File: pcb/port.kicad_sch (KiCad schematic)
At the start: 0 parts

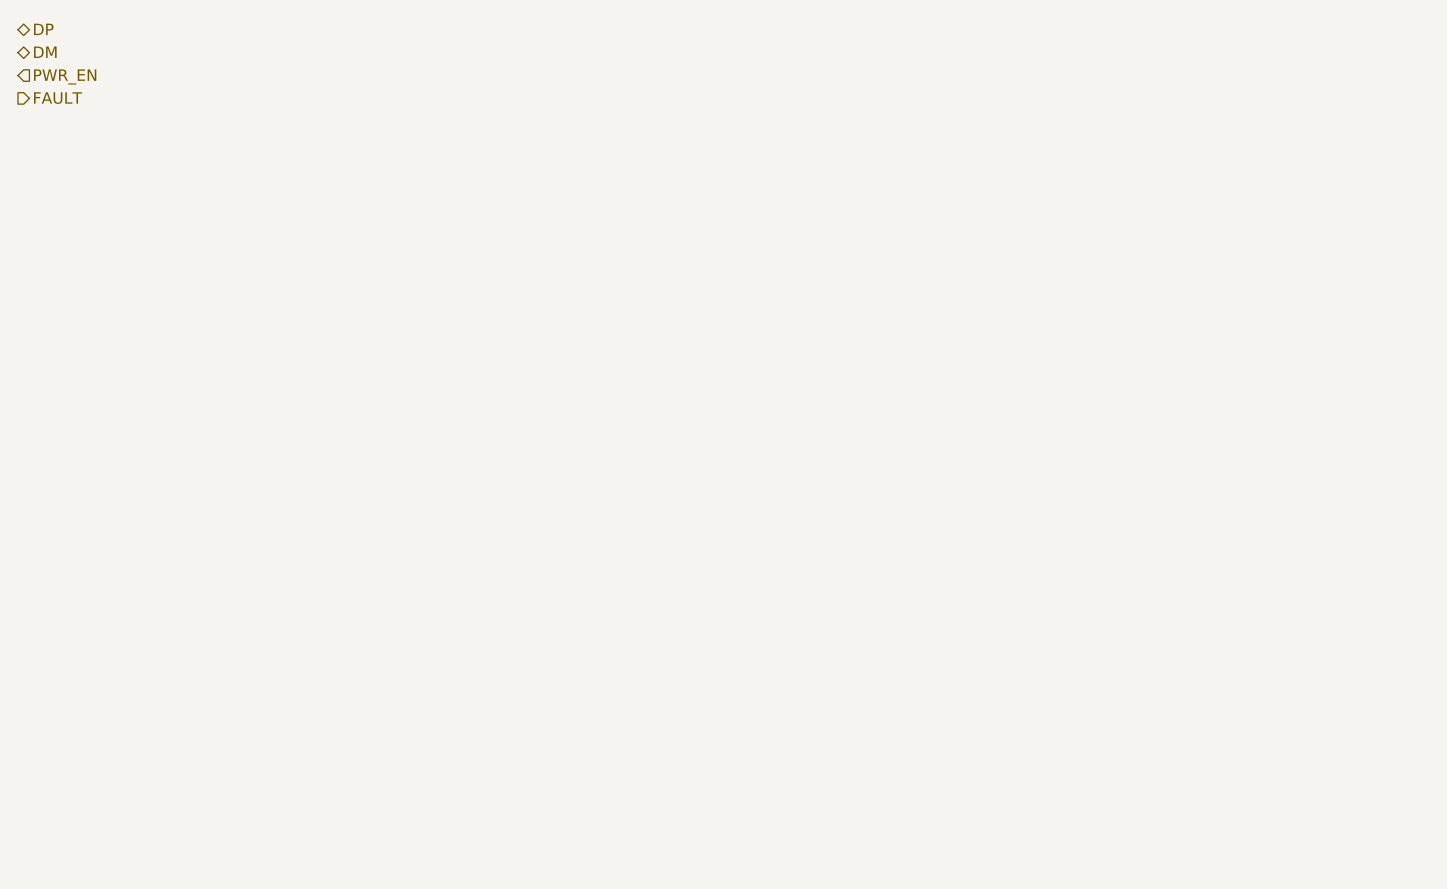
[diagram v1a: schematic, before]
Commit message: draw the port, once, and place it four times
The current-limited switch, the ESD array, the receptacle and the bulk
capacitance. Left to right: the hub's enable arrives, the switch passes 5 V
through, the array protects the pair on its way out, and the receptacle is the
board edge. The fault goes straight back to the hub, which pulls it up itself.

The rails are drawn rather than scattered. Giving every ground pin its own
symbol is quick to generate and tiresome to read -- the sheet fills with
identical glyphs and the shape of the supply disappears -- so the generator now
draws one line, one symbol and a drop to each pin. Same netlist, a tenth of the
symbols. That is the change that was asked for after the same tidying had been
done by hand twice.

Three bugs had to be found on the way, and the first two hid the third.

A symbol may be mirrored, because a connector drawn with its pins facing out of
the package has them facing the wrong way at the right-hand edge of a sheet, and
turning it over instead would reverse the pin order that the pair has to line up
with. The mirror flag was first built as a string of escape sequences and passed
through a plain substitution, which does not interpret them: the literal
characters went into the file, the symbol was malformed, and KiCad stopped
reading the sheet at that point. What it reported was that the sheet had no
hierarchical labels -- which was true, in the sense that it had never got to
them.

The per-placement references then leaked into the reference field itself, which
belongs to one reference; the list belongs only in the instance paths.

And the placements were being read in file order, which the editor is free to
change when it saves -- it had already put them in the order 4, 3, 1, 2. The
references now follow the sheet names, and the generator refuses to run if it
does not find exactly four.

Co-Authored-By: Claude Opus 5 (1M context) <noreply@anthropic.com>
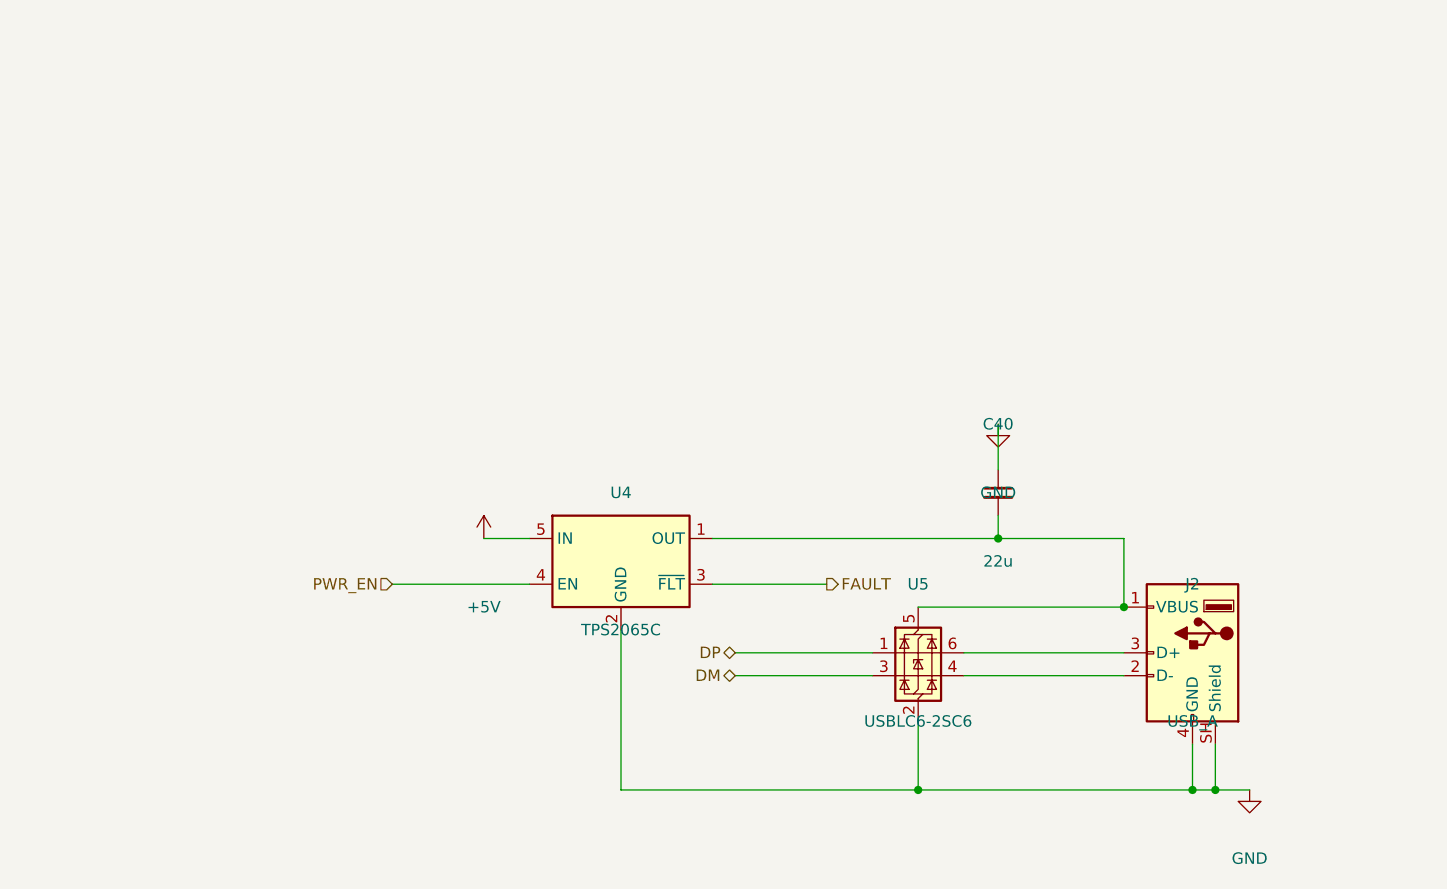
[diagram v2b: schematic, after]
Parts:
- added C40: 22u, symbol Device:C_Small
- added J2: USB_A, symbol Connector:USB_A
- added U4: TPS2065C, symbol Power_Management:TPS2065CDBV
- added U5: USBLC6-2SC6, symbol Power_Protection:USBLC6-2SC6
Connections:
- net DM: now also U5.3 (I/O2)
- net DP: now also U5.1 (I/O1)
- net FAULT: now also U4.3 (~{FLT})
- net PWR_EN: now also U4.4 (EN)
- new net: J2.2 (D-), U5.4 (I/O2)
- new net: C40.2, J2.1 (VBUS), U4.1 (OUT), U5.5 (VBUS)
- new net: J2.3 (D+), U5.6 (I/O1)
- new net +5V: U4.5 (IN)
- new net GND: C40.1, J2.4 (GND), J2.SH (Shield), U4.2 (GND), U5.2 (GND)

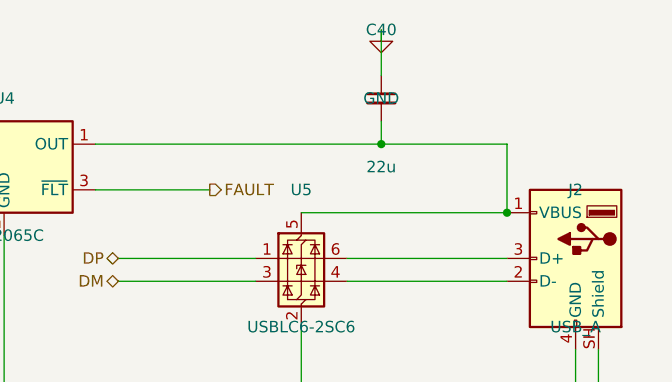
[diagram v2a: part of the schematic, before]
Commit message: draw the data port, and let its pinout answer an open question
The receptacle, the terminations that tell a source what we are, the protection
array, the sense divider the firmware reads to know a host is there, and the
diode through which the rail takes its capped contribution. Both halves of each
data pair are tied, which is what lets the cable go in either way up -- four pin
points, not two, and the netlist is the only place that shows it was done.

Reading the PD sink's pinout to draw the other upstream sheet answered a
question that was down as needing the datasheet by eye. It has no internal
output switch to open: it brings out a gate drive for an external FET. So the
blocking that keeps the data port from back-driving an exposed connector is ours
to design rather than someone else's arrangement to trust, and the open item
becomes an orientation choice. The same pinout shows the requested voltage and
current are resistor-settable as well as addressable, so the profile has a
hardware default before any firmware runs -- worth having on a board whose
firmware is the thing being updated.

The power sheet is NOT drawn, and deliberately. Its three converters each need
numbers this toolchain cannot read: which resistor sets the charger's current
programming against its input-limit pin, and how to tell the boost's feedback
divider apart from its current-limit and frequency resistors. The vendor
publishes both with the pin tables and design equations in a form that extracts
at four and thirty per cent. The topology is understood; the values are not, and
a wrong number in the supply is expensive, so it is recorded as needing a human
with the PDF open rather than drawn from inference.

Co-Authored-By: Claude Opus 5 (1M context) <noreply@anthropic.com>
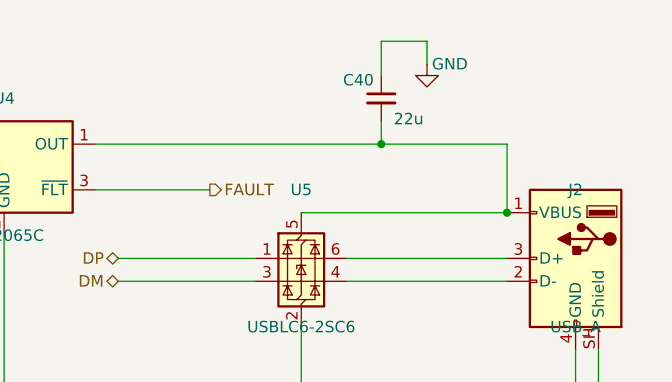
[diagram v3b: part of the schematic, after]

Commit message: specify every capacitor: a rating and a dielectric, chosen from its net
A value on its own is not a specification. Each of the 62 capacitor symbols now carries a voltage
rating and a dielectric picked from the net it sits on -- at least twice the working voltage,
rounded to a standard rating, and never below what a socket the user can reach can present. Both
are hidden fields, so the drawing stays readable and a bill of materials can still be made from it.

Two of the choices are decisions rather than arithmetic.

The connector-side parts are rated for abuse at 50V, because nothing on the board protects them:
both input switches sit downstream of them, so the sink's own supply decoupling and the data
port's see whatever a hostile charger produces with no switch in between.

The charger's input bank is rated 25V on a condition, and the condition is firmware. The input
over-voltage trip defaults to 26V, which is above a 25V part, so rating the bank for its working
voltage is only safe if that trip comes down. The part offers 7V, 12V, 22V and 26V and 12V is the
right one here: the sink never asks for more than 9V, so 12V clears the profile with room and
bounds what the bank can ever see. A board decision that creates a firmware requirement is exactly
the sort that gets lost, so it is recorded on both sides.

What is left open is what the banks are worth once fitted. The charger specifies them as counts of
10uF parts, which only means something if each part is still worth 10uF where it sits, and a
ceramic at 9V is not. The rating and the dielectric are settled; the package is not, and the
package is what decides how much survives. The footprint step has to read each chosen part's bias
curve and add parts if the effective value falls short rather than assume the count was the point.
That is the one piece of this specification that can still change the part count.

Rules check unchanged, and the schematic check is clean.

Co-Authored-By: Claude Opus 5 (1M context) <norepl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
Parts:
- C40: Dielectric (none) -> X7R; Voltage (none) -> 25V
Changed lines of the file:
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@@
+			)
+		)
+		(property "Voltage" "25V"
+			(at 171.958 93.726 0)
+			(show_name no)
+			(do_not_autoplace no)
+			(effects
+				(font
+					(size 1.27 1.27)
+				)
+				(hide yes)
+			)
+		)
+		(property "Dielectric" "X7R"
+			(at 171.958 93.726 0)
+			(show_name no)
+			(do_not_autoplace no)
+			(effects
+				(font
+					(size 1.27 1.27)
+				)
+				(hide yes)
 			)
 		)

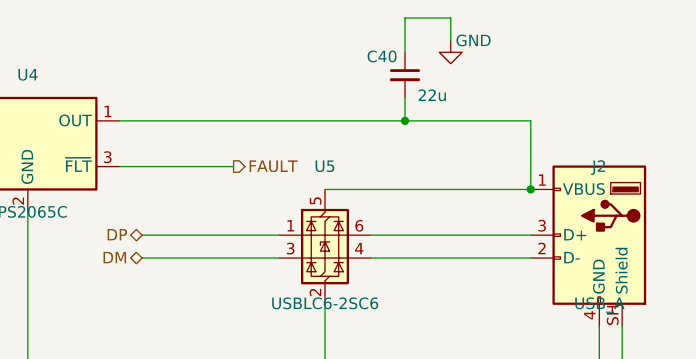
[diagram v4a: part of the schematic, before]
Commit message: calculate the capacitor banks, and give every one of them a package
The question a value and a rating leave open is how much capacitance is actually there once the
voltage is across it, and the answer differs by package for the same value and rating. So the
requirement is derived bank by bank rather than taken from the vendors' part counts.

The charger's input is the binding case. Holding its input ripple to 100 mV with 5.4 A through the
inductor needs 8.6uF in circuit out of the 20uF fitted, so 43% has to survive 9V. The 5V rail needs
36% of what it carries and the system rail 27%. That last one is worth stating properly: ripple
alone would want only 2.5uF there, so the bank exists to answer load steps, and the realistic fast
step is the radio transmitting and the processor waking rather than the ports, which cannot step
quickly because the boost soft-starts over 4ms. At half an amp over five microseconds that is 25uF
against about 70uF effective.

43% is comfortable in 1206 and marginal in 0603 for a 10uF part at 9V, so the five capacitors on
the 9V nodes take 1206 and everything at 4.5V or under takes 0805. Decoupling goes to 0402, where
being near the pin matters more than the package, and the frequency- and loop-setting parts to
0603, where there is nothing to derate.

The answer to the open item is that the counts do not change: every bank is adequate as drawn
provided each part keeps roughly half of itself, which is what the package choice delivers. What is
left is a purchasing check rather than a design one.

Two asymmetries recorded. The 3.3V converter's vendor states that its recommended values anticipate
tolerance and bias derating and quotes 20% and 50%, so its table is nominal with the margin already
in it; the charger's and the boost's say nothing, so there the derating is ours to carry. And the
processor specifies an effective tolerance rather than a nominal one -- its core regulator's output
capacitor must be 4.7uF +/-20% in circuit.

The checker's 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
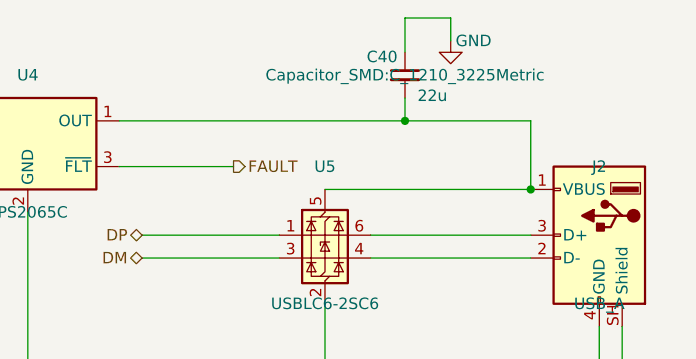
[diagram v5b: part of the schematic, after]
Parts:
- C40: footprint (none) -> Capacitor_SMD:C_1210_3225Metric
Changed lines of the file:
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@@
 			)
 		)
-		(property "Footprint" ""
+		(property "Footprint" "Capacitor_SMD:C_1210_3225Metric"
 			(at 168.91 91.44 0)
 			(show_name no)

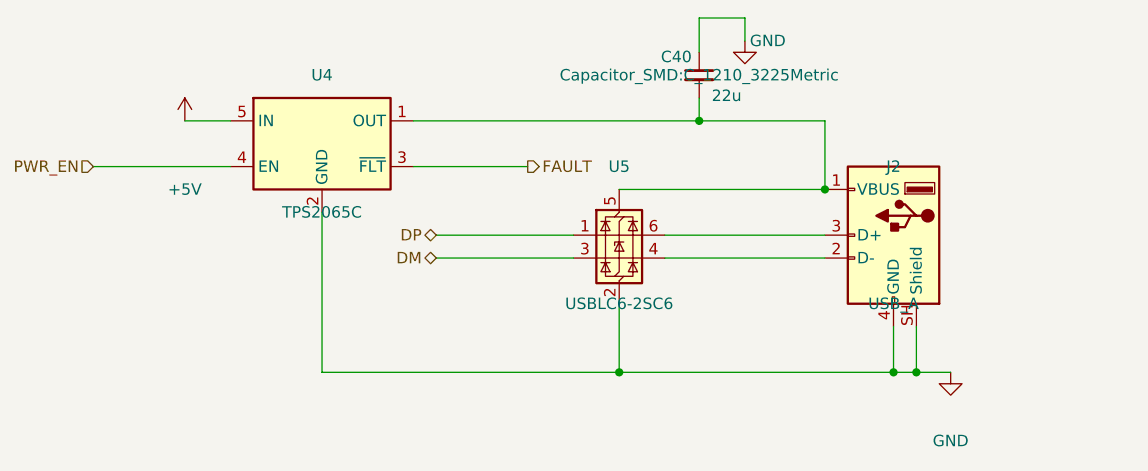
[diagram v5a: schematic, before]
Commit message: assign the footprints, and take the radio module's from its vendor
132 of the 135 parts now carry a footprint. Most follow from the package, the capacitors' follow
from the bias calculation, and the resistors are 0603 rather than 0402 because the board has room,
the first one runs bare on a bench, and a part you can get a probe or an iron onto is worth more
there than the millimetre it saves.

The radio module nearly went in hand-drawn. It has no footprint in any stock library, so the
obvious move was to draw one from the dimension drawing in its datasheet; the pitch, pad size and
pad length read off cleanly, but where each pad sits along its edge did not, and what I had was
inference from where things appeared in a rendered figure rather than a stated number. Raspberry Pi
publish a KiCad symbol and footprint, so that is what is fitted, in a project footprint library
beside the project symbol library. The figure agreed on everything it stated plainly, which says
nothing about the parts it did not.

Taking the official symbol also checked this project's hand-drawn one against theirs. All 21 pins
agree. Four carry different names -- their DI and DO, their nIRQ and WL_ON -- and nothing else
differs, so the pin numbering derived from the module's table is confirmed against its author
rather than merely self-consistent.

Four packages are fitted provisionally and are recorded as such, because what is unsettled about
them is invisible: the processor, the hub, the 3.3V converter and the power sink are in packages
whose library entries differ only in the size of the pad under the part. Body, pitch and pin count
are right; the pad is the nearest variant and wants checking against each vendor's land pattern,
since too small costs thermal performance and too large can wick the part off its pins.

Three parts are deliberately left without one. For the remaining inductors the footprint is the
part -- pad geometry differs between vendors at the same nominal size -- so choosing an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
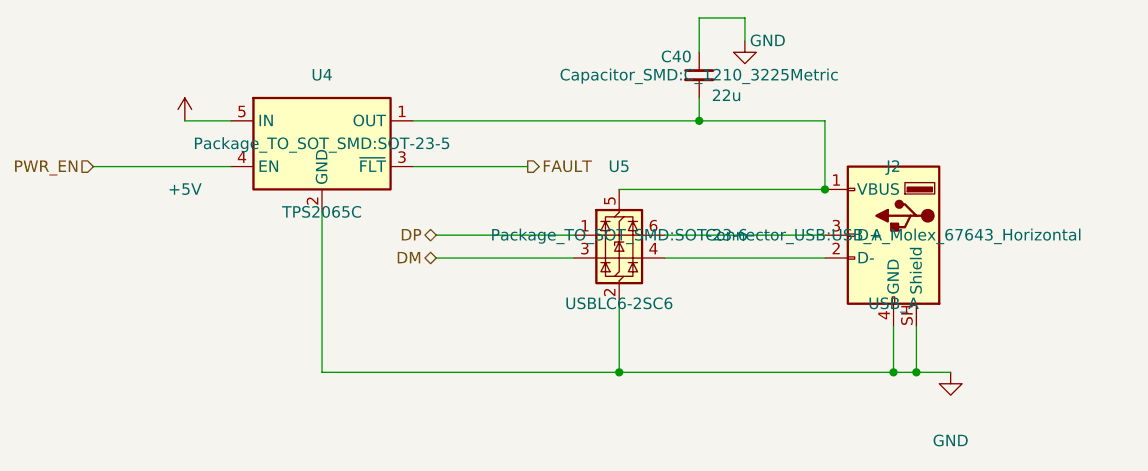
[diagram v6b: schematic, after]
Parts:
- J2: footprint (none) -> Connector_USB:USB_A_Molex_67643_Horizontal
- U4: footprint (none) -> Package_TO_SOT_SMD:SOT-23-5
- U5: footprint (none) -> Package_TO_SOT_SMD:SOT-23-6
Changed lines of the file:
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@@
 			)
 		)
-		(property "Footprint" ""
+		(property "Footprint" "Package_TO_SOT_SMD:SOT-23-6"
 			(at 160.02 109.22 0)
 			(show_name no)
@@
 			)
 		)
-		(property "Footprint" ""
+		(property "Footprint" "Connector_USB:USB_A_Molex_67643_Horizontal"
 			(at 190.5 109.22 0)
 			(show_name no)
@@
 			)
 		)
-		(property "Footprint" ""
+		(property "Footprint" "Package_TO_SOT_SMD:SOT-23-5"
 			(at 127 99.06 0)
 			(show_name no)
